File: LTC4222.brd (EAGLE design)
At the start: 100 x 80 mm, 26 parts, among them J1 67997-100HLF, Q1 PMV15ENEAR, Q2 PMV15ENEAR

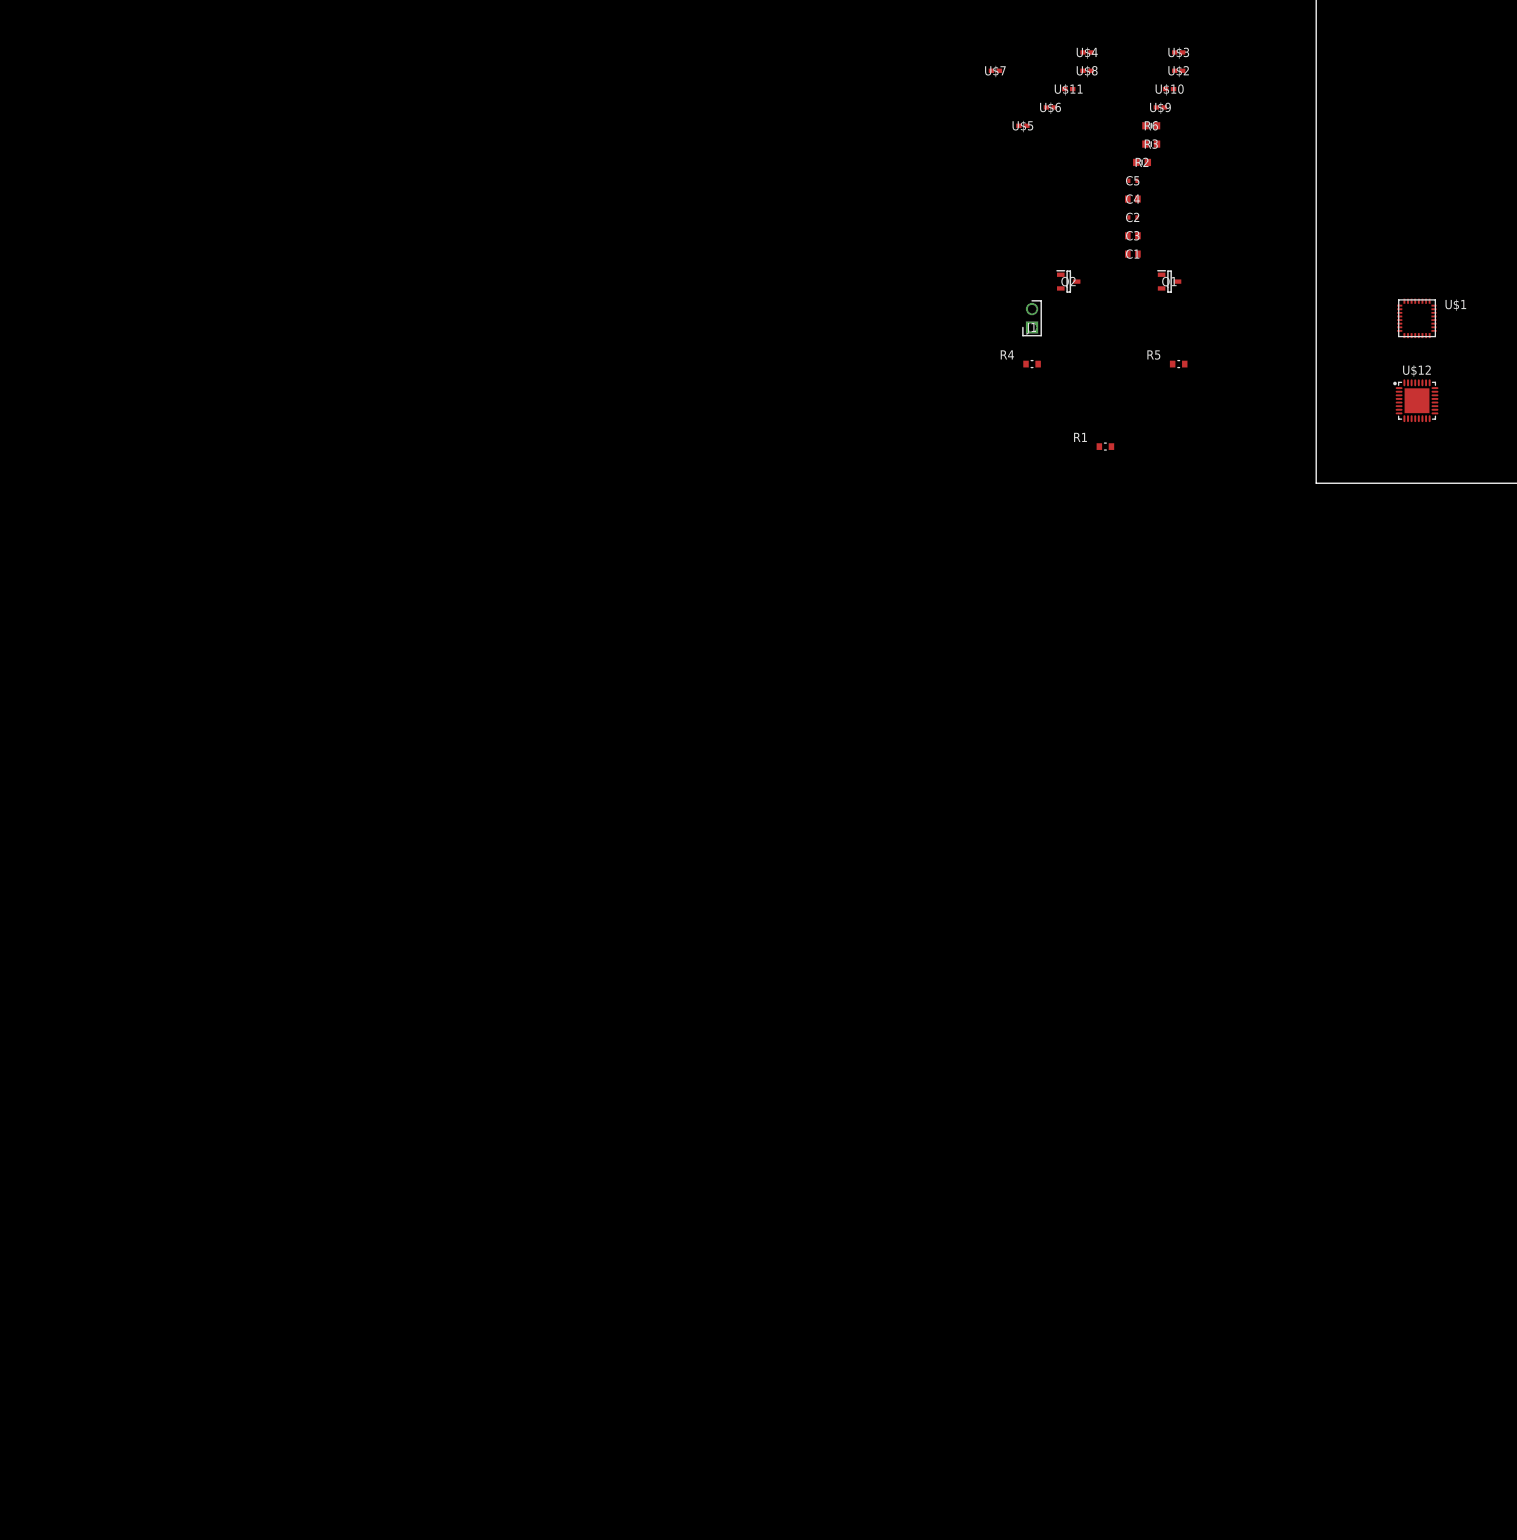
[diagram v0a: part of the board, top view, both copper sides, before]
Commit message: LTC4222 Version 1.0 w/o flip flop
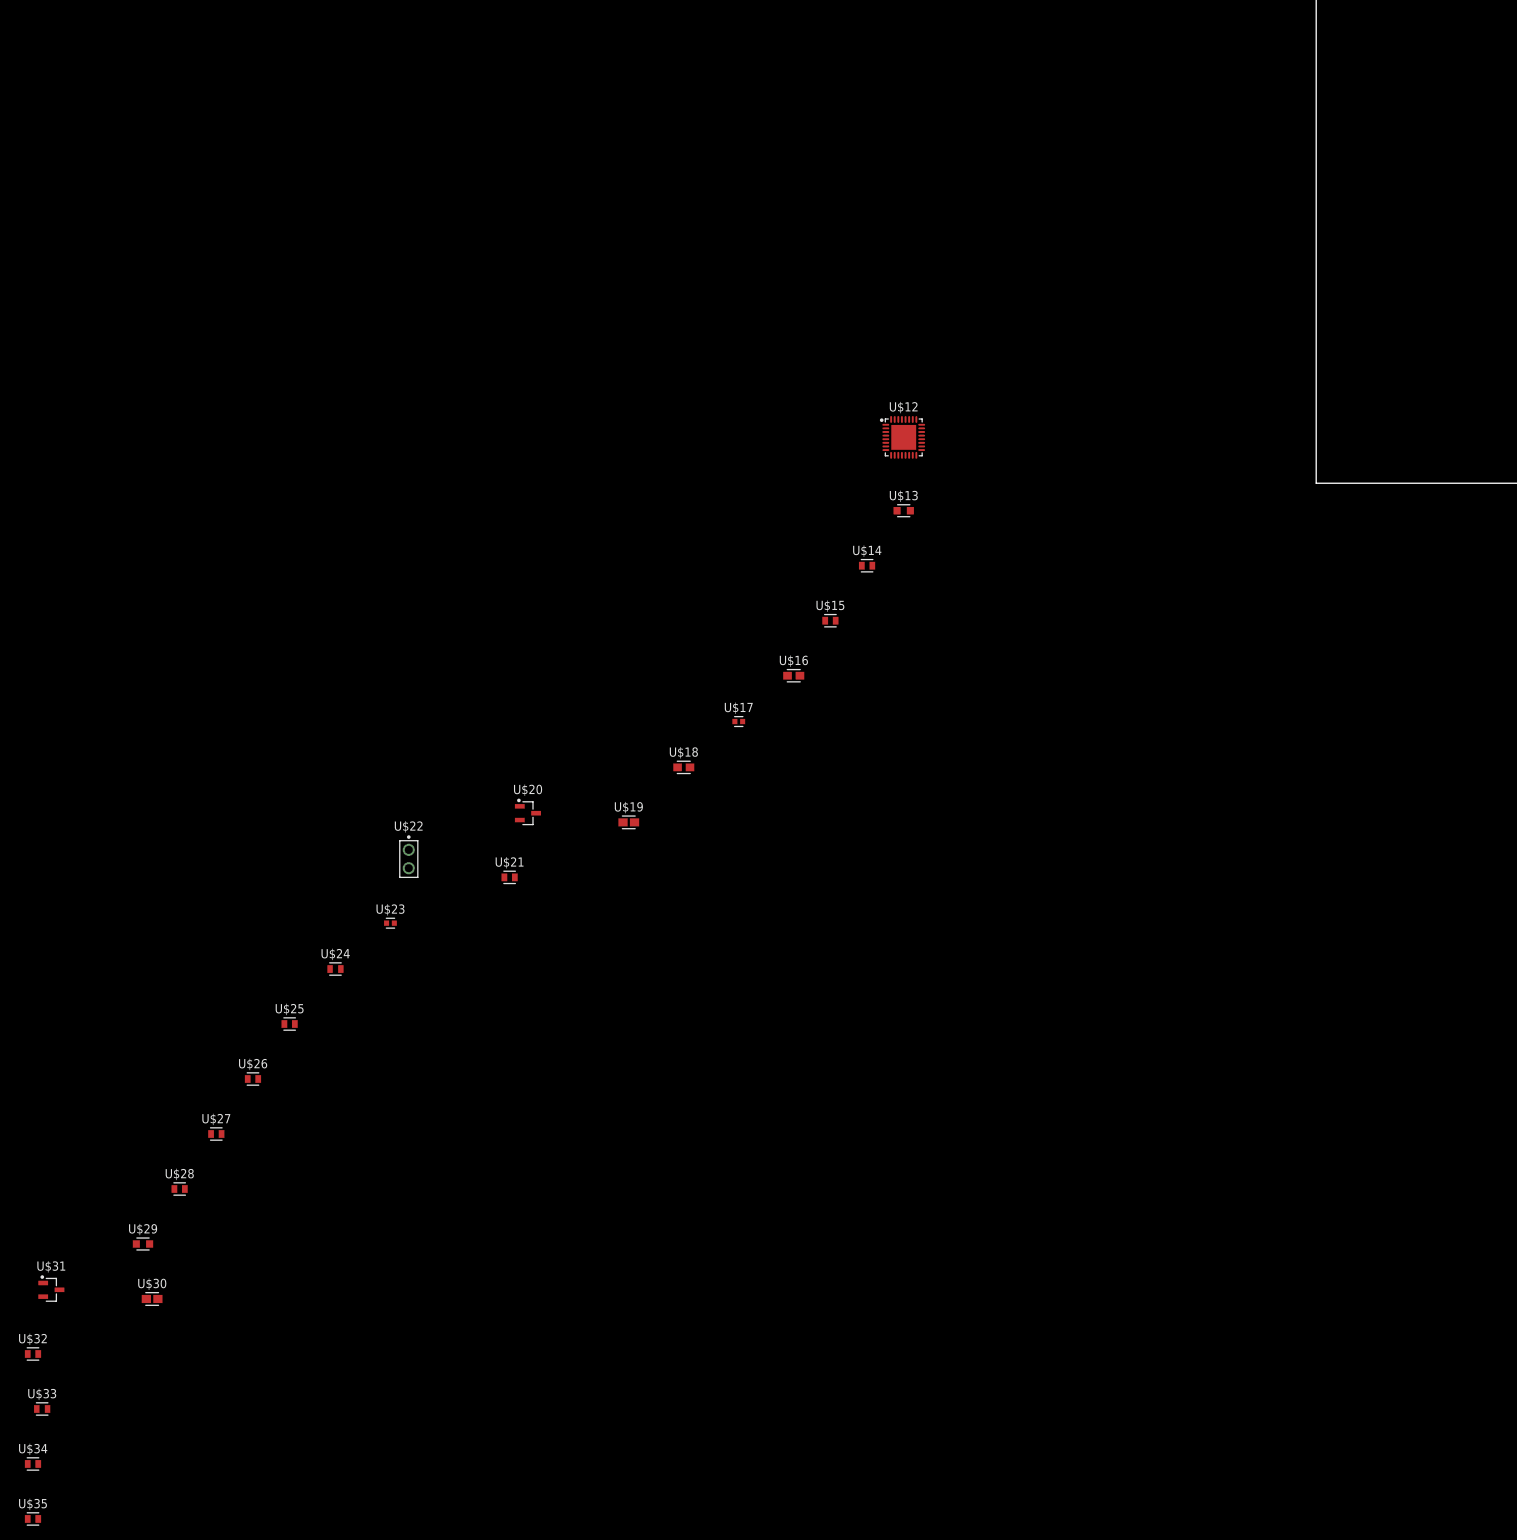
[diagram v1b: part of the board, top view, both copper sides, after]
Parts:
- removed C1, C3: CGA3E2X7R1H104K080AE, SamacSys_Parts:CAPC1608X90N
- removed C2: CGA2B3X7R1V223K050BB, SamacSys_Parts:CAPC1005X55N
- removed C4: CGA3E1X7R1V105K080AE, SamacSys_Parts:CAPC1608X90N
- removed C5: CGA2B3X7R1E683K050BB, SamacSys_Parts:CAPC1005X55N
- removed J1: 67997-100HLF, SamacSys_Parts:HDRV2W67P254_2X1_254X483X858P
- removed Q1, Q2: PMV15ENEAR, SamacSys_Parts:SOT95P230X110-3N
- removed R1, R5: TNPW060310R0BEEN, SamacSys_Parts:RESC1608X60N
- removed R2: MCT0603PD4991DP500, SamacSys_Parts:RESC1608X55N
- removed R3, R6: TNPW060310K0BEEA, SamacSys_Parts:RESC1608X55N
- removed R4: TNPW06031K02BEEA, SamacSys_Parts:RESC1608X60N
- removed U$1: DUMMY_LTC, SamacSys_Parts:DUMMY_LTC
- removed U$10: 10.2K_DUMMY, SamacSys_Parts:34KOHMDUMMY
- removed U$11, U$6: 3.57K_DUMMY, SamacSys_Parts:34KOHMDUMMY
- removed U$2: 1.8K_DUMMY, SamacSys_Parts:34KOHMDUMMY
- removed U$3: 392_DUMMY, SamacSys_Parts:34KOHMDUMMY
- removed U$4: 953_DUMMY, SamacSys_Parts:34KOHMDUMMY
- removed U$5, U$9: 18MILLI_DUMMY, SamacSys_Parts:34KOHMDUMMY
- removed U$7: 34K_DUMMY, SamacSys_Parts:34KOHMDUMMY
- removed U$8: 3.4K_DUMMY, SamacSys_Parts:34KOHMDUMMY
- added U$13: AT0603DRD071K82L, Baja_Parts_Lib:RESC1608X45M
- added U$14: TNPW0603392RBEEA, Baja_Parts_Lib:AT0603
- added U$15: TNPW0603953RBEEA, Baja_Parts_Lib:AT0603
- added U$16: CGA3E1X7R1V105K080AE, Baja_Parts_Lib:CAPC1608X80M
- added U$17: CGA2B3X7R1E683K050BB, Baja_Parts_Lib:CAPC1005X50M
- added U$18: CGA3E2X7R1H104K080AE, Baja_Parts_Lib:CAPC1608X80M
- added U$19, U$30: WSL0603R0180FEA, Baja_Parts_Lib:RESC1507X40M
- added U$20, U$31: PMV15ENEAR, Baja_Parts_Lib:SOT95P230X110-3M
- added U$21, U$32: TNPW060310R0BEEN, Baja_Parts_Lib:AT0603
- added U$22: 67997-100HLF, Baja_Parts_Lib:HDRV2W64P254_2X1_241X508X838B
- added U$23: CGA2B3X7R1V223K050BB, Baja_Parts_Lib:CAPC1005X50M
- added U$24, U$33: MCT0603PD4991DP500, Baja_Parts_Lib:RESC1508X47M
- added U$25, U$34: TNPW06033K57BEEA, Baja_Parts_Lib:AT0603
- added U$26, U$35: TNPW060310K0BEEA, Baja_Parts_Lib:AT0603
- added U$27: TNPW060334K0BEEA, Baja_Parts_Lib:AT0603
- added U$28: TNPW06031K02BEEA, Baja_Parts_Lib:AT0603
- added U$29: AT0603DRD073K4L, Baja_Parts_Lib:RESC1608X45M
- moved U$12 71.3 mm to (-57.1, 6.35)
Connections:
- removed net 0: C1.2, C3.2, C4.1, C5.1, U$1.P$4, U$11.2, U$4.2, U$6.2, U$8.2
- removed net N$1: C1.1, U$1.P$2, U$1.P$3, U$1.P$7
- removed net N$10: R2.2, U$1.P$15, U$6.1
- removed net N$11: R3.2, U$1.P$16
- removed net N$12: C3.1, R4.1, U$1.P$32, U$7.2
- removed net N$13: R4.2, U$1.P$31, U$8.1
- removed net N$14: U$1.P$30, U$7.1, U$9.1
- removed net N$15: Q2.3, U$1.P$29, U$9.2
- removed net N$16: Q2.1, R5.1
- removed net N$17: R5.2, U$1.P$28
- removed net N$18: Q2.2, R6.1, U$1.P$27, U$10.1
- removed net N$19: U$1.P$26, U$10.2, U$11.1
- removed net N$2: U$1.P$9, U$3.2, U$4.1
- removed net N$20: U$1.P$17, U$1.P$24
- removed net N$21: R6.2, U$1.P$25
- removed net N$22: C4.2, U$1.P$8
- removed net N$23: C5.2, U$1.P$1
- removed net N$3: U$1.P$10, U$2.2, U$3.1
- removed net N$4: U$1.P$11, U$2.1, U$5.1
- removed net N$5: Q1.3, U$1.P$12, U$5.2
- removed net N$6: J1.1, Q1.1, R1.1
- removed net N$7: R1.2, U$1.P$13
- removed net N$8: C2.2, J1.2
- removed net N$9: C2.1, Q1.2, R2.1, R3.1, U$1.P$14
- new net GND: U$12.4, U$15.2, U$16.1, U$17.1, U$18.1, U$25.2, U$29.2, U$34.2
- new net N$24: U$12.10, U$13.2, U$14.1
- new net N$25: U$12.9, U$14.2, U$15.1
- new net N$26: U$12.8, U$16.2
- new net N$27: U$12.1, U$17.2
- new net N$28: U$12.12, U$19.1, U$20.3
- new net N$29: U$12.2, U$12.3, U$12.7, U$18.2
- new net N$30: U$12.11, U$13.1, U$19.2
- new net N$31: U$20.1, U$21.1, U$22.1
- new net N$32: U$12.13, U$21.2
- new net N$33: U$22.2, U$23.2
- new net N$34: U$12.14, U$20.2, U$23.1, U$24.1, U$26.1
- new net N$35: U$12.15, U$24.2, U$25.1
- new net N$36: U$12.32, U$28.2, U$29.1
- new net N$37: U$12.16, U$26.2
- new net N$38: U$12.31, U$27.2, U$28.1
- new net N$39: U$12.30, U$27.1, U$30.1
- new net N$40: U$12.29, U$30.2, U$31.2
- new net N$41: U$31.1, U$32.1
- new net N$42: U$12.28, U$32.2
- new net N$43: U$12.27, U$31.3, U$33.1, U$35.1
- new net N$44: U$12.25, U$35.2
- new net N$45: U$12.26, U$33.2, U$34.1
